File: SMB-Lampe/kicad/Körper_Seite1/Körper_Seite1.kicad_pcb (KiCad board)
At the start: 2 copper layers, 123 x 95.7 mm, 24 parts, among them J1 Conn_01x01_Pin, J2 Conn_01x01_Pin, J3 Conn_01x01_Pin, J4 Conn_01x01_Pin, J5 Conn_01x01_Pin, J6 Conn_01x01_Pin

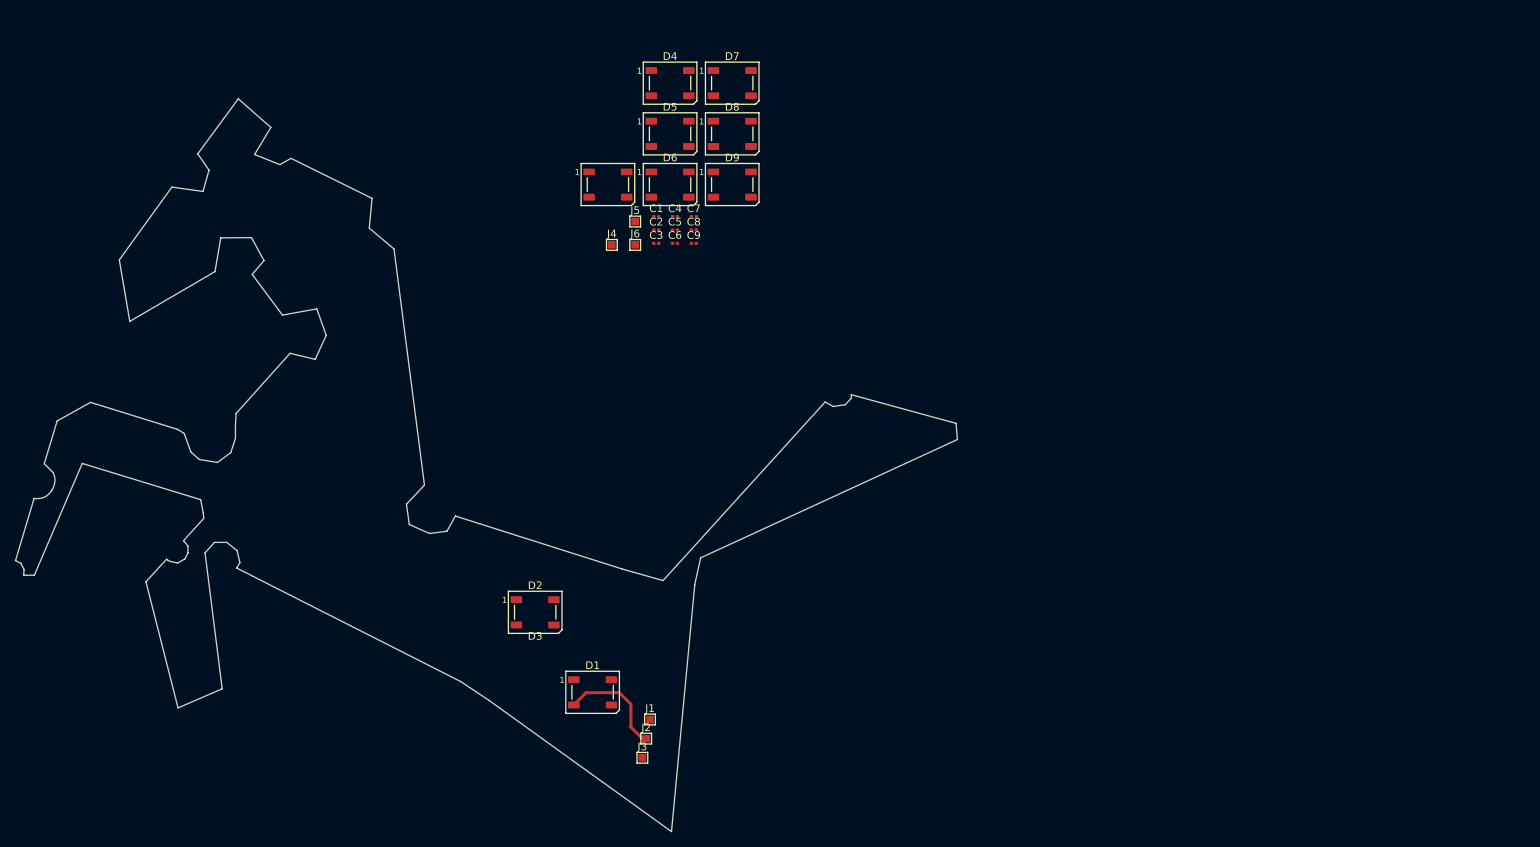
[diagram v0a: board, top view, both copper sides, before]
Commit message: Platine für Körper Seite 1 erfolgreich erstellt
Die Platine wurde mit der alten Außenkontur erstellt und fast komplett erfolgreich die Leiterbahnen erstellt.
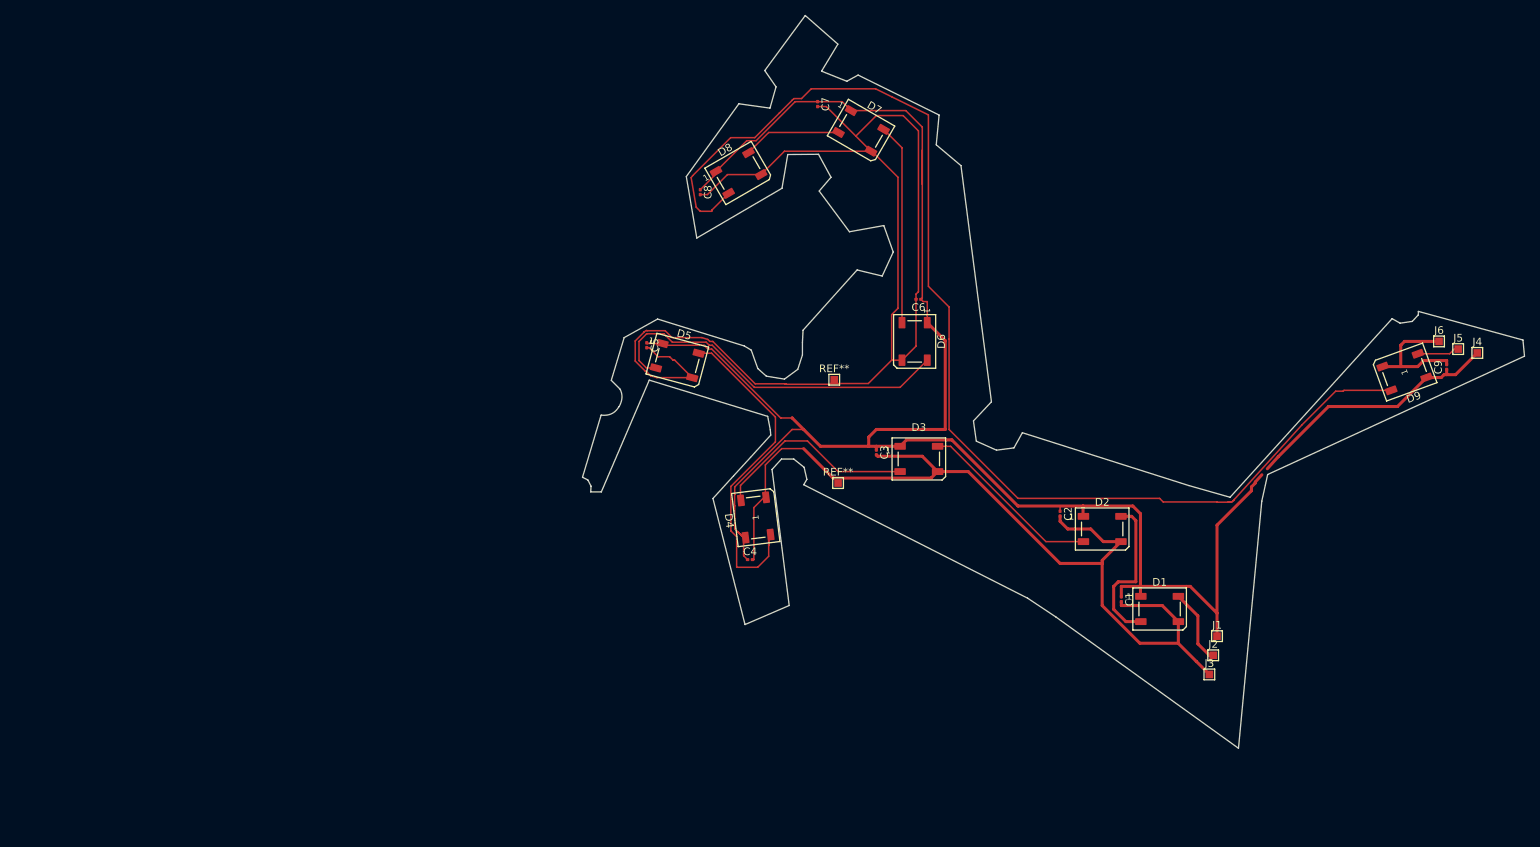
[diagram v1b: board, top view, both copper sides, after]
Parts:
- added REF**: TestPoint_Pad_1.0x1.0mm, TestPoint:TestPoint_Pad_1.0x1.0mm, F.Cu at (188.1, 95.1)
- added REF**: TestPoint_Pad_1.0x1.0mm, TestPoint:TestPoint_Pad_1.0x1.0mm, F.Cu at (187.6, 81.6)
- moved J4 113.9 mm to (271.6, 78.1)
- moved J5 108.8 mm to (269.1, 77.6)
- moved J6 105.8 mm to (266.6, 76.6)
- moved C9 99.7 mm to (267.6, 80.0), turned to 90 degrees
- moved D9 91.2 mm to (262.1, 80.6), turned to -160 degrees
- moved C1 78.7 mm to (225.1, 110.3), turned to -90 degrees
- moved D1 74.9 mm to (230.1, 111.6)
- moved D2 74.9 mm to (222.6, 101.1)
- moved J1 74.9 mm to (237.6, 115.1)
- moved J2 74.9 mm to (237.1, 117.6)
- moved J3 74.9 mm to (236.6, 120.1)
- moved C2 64.5 mm to (217.1, 99.1), turned to -90 degrees
- moved D4 57.8 mm to (177.3, 99.6), turned to 97 degrees
- moved D3 54.2 mm to (198.6, 92.0)
- moved C4 45.9 mm to (176.6, 105.1)
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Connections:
- D1 pad 2: /Data_In -> Net-(D1-DOUT)
- D1 pad 4: Net-(D1-DIN) -> /Data_In
- D2 pad 2: Net-(D1-DIN) -> Net-(D2-DOUT)
- D2 pad 4: Net-(D2-DIN) -> Net-(D1-DOUT)
- D3 pad 2: Net-(D2-DIN) -> Net-(D3-DOUT)
- D3 pad 4: Net-(D3-DIN) -> Net-(D2-DOUT)
- D4 pad 2: Net-(D3-DIN) -> Net-(D4-DOUT)
- D4 pad 4: Net-(D4-DIN) -> Net-(D3-DOUT)
- D5 pad 2: Net-(D4-DIN) -> Data
- D5 pad 4: Data -> Net-(D4-DOUT)
- D6 pad 2: Data -> Net-(D6-DOUT)
- D6 pad 4: Net-(D6-DIN) -> Data
- D7 pad 2: Net-(D6-DIN) -> Net-(D7-DOUT)
- D7 pad 4: Net-(D7-DIN) -> Net-(D6-DOUT)
- D8 pad 2: Net-(D7-DIN) -> Net-(D8-DOUT)
- D8 pad 4: Net-(D8-DIN) -> Net-(D7-DOUT)
- D9 pad 2: Net-(D8-DIN) -> /Data_OUT
- D9 pad 4: /Data_OUT -> Net-(D8-DOUT)
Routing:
- net GND: track 0.00 -> 301.9 mm
- net +5V: track 0.00 -> 283.3 mm
- net Net-(D8-DOUT): track 0.00 -> 156.3 mm
- net Data: track 0.00 -> 47.5 mm
- net Net-(D4-DOUT): track 0.00 -> 44.8 mm
- net Net-(D3-DOUT): track 0.00 -> 26.7 mm
- net Net-(D6-DOUT): track 0.00 -> 26.2 mm
- net Net-(D2-DOUT): track 0.00 -> 24.2 mm
- net Net-(D1-DOUT): track 0.00 -> 20.5 mm
- net Net-(D7-DOUT): track 0.00 -> 12.9 mm
- net /Data_OUT: track 0.00 -> 5.52 mm
- net /Data_In: track 14.4 -> 9.88 mm
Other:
- board size 123 x 95.7 mm -> 123.1 x 95.7 mm

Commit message: Hinterbein Seite 1/2 erstellt
Anschlüsse zwischen den Platinen mit MountingHoles. Eigenes MountingHole Erstellt
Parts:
- moved J4 128.4 mm to (143.3, 83.4)
- moved J5 128.4 mm to (140.8, 82.9)
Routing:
- net /Data_OUT: track 5.52 -> 54.0 mm
- net +5V: track 283.3 -> 325.1 mm
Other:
- board size 123.1 x 95.7 mm -> 252 x 99.5 mm

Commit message: Vorderseite Platine Körper Seite 1 fertig
zwei GND Verbindungen fehlen noch
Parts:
- removed J4, J5, J6: Conn_01x01_Pin, TestPoint:TestPoint_Pad_1.0x1.0mm
- removed REF** (x2): TestPoint_Pad_1.0x1.0mm, TestPoint:TestPoint_Pad_1.0x1.0mm
- added H1: MountingHole_Pad, Eigenen_Library:MountingHole D2 x d1 test, F.Cu at (189.0, 101.0)
- added H2: MountingHole_Pad, Eigenen_Library:MountingHole D2 x d1 test, F.Cu at (186.0, 100.0)
- added H3: MountingHole_Pad, Eigenen_Library:MountingHole D2 x d1 test, F.Cu at (183.0, 99.0)
- J1, J2, J3: footprint TestPoint:TestPoint_Pad_1.0x1.0mm -> TestPoint:TestPoint_Pad_2.0x2.0mm
- moved C3 89.5 mm to (106.0, 112.0)
- moved D3 89.5 mm to (111.5, 112.5)
- moved J3 88.7 mm to (151.0, 143.5)
- moved C5 88.4 mm to (77.8, 100.4), turned to -109 degrees
- moved D6 88.1 mm to (112.5, 97.5)
- moved J2 88.0 mm to (152.0, 140.0)
- moved C6 87.9 mm to (113.2, 92.0)
- moved D9 87.9 mm to (177.5, 104.5), turned to -154 degrees
- moved D5 87.8 mm to (82.2, 102.0), turned to -18 degrees
- moved C2 87.7 mm to (132.5, 122.5)
- moved D4 87.7 mm to (92.7, 122.8)
- moved D7 87.6 mm to (106.5, 72.0), turned to -45 degrees
- moved C9 87.5 mm to (183.0, 102.5), turned to 115 degrees
- moved D8 87.5 mm to (90.8, 78.4), turned to 29 degrees
- moved D2 87.4 mm to (138.0, 123.0)
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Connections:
- net /Data_In renamed /Data_In__Hinterbein_hinten_Seite2
- D9 pad 2: /Data_OUT -> /Data_OUT_Körper_Seite2
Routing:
- net /Data_OUT: track 54.0 -> 0.00 mm
- net +5V: track 325.1 -> 285.8 mm
- net /Data_OUT_Körper_Seite2: track 0.00 -> 7.83 mm
- net Net-(D4-DOUT): track 44.8 -> 51.3 mm
- net GND: track 301.9 -> 295.6 mm
- net Net-(D2-DOUT): track 24.2 -> 29.5 mm
- net Net-(D3-DOUT): track 26.7 -> 21.8 mm
- net Net-(D6-DOUT): track 26.2 -> 23.1 mm
- net Data: track 47.5 -> 49.9 mm
- net Net-(D1-DOUT): track 20.5 -> 22.8 mm
- net Net-(D8-DOUT): track 156.3 -> 157.8 mm
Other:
- board size 252 x 99.5 mm -> 121.9 x 96.3 mm
- board text added: "-155°"
- board text added: "-18°"
- board text added: "29°"
- board text added: "97°"

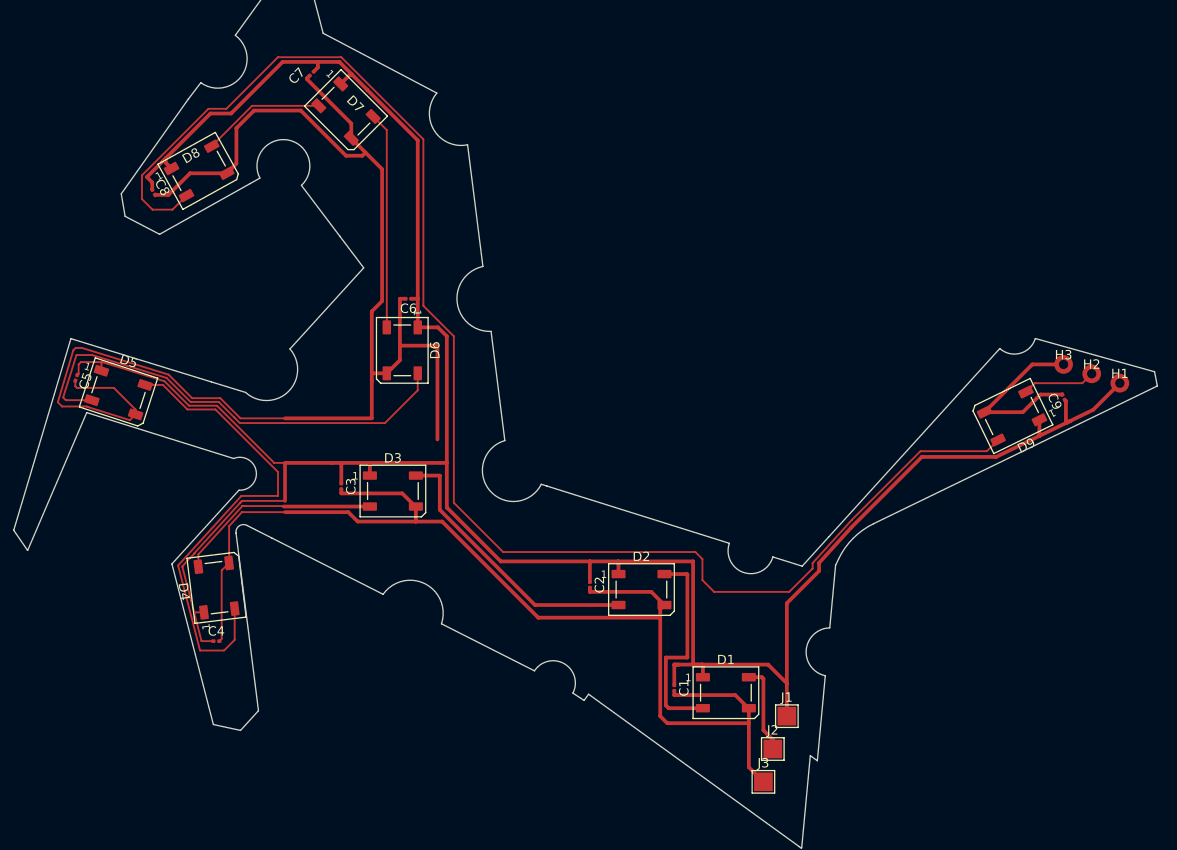
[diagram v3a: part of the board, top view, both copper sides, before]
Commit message: Körper mit Vorder und Rückseite fertig
Alle Leiterbahnen sind gelegt und Verbindungen zu den anderen Platinen platziert
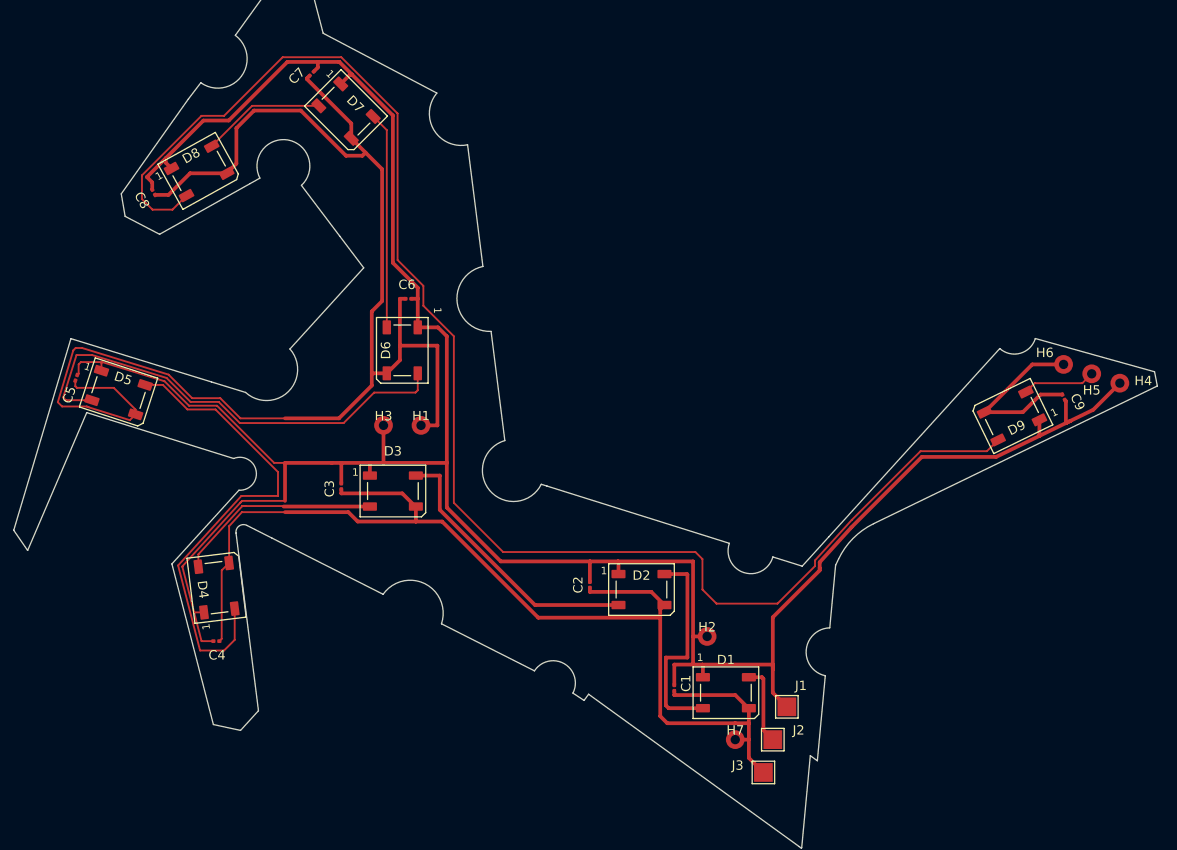
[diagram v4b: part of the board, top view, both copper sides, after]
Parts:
- added H1: MountingHole_Pad, Eigenen_Library:MountingHole D2 x d1 test, F.Cu at (114.5, 105.5)
- added H2: MountingHole_Pad, Eigenen_Library:MountingHole D2 x d1 test, F.Cu at (145.0, 128.0)
- added H3: MountingHole_Pad, Eigenen_Library:MountingHole D2 x d1 test, F.Cu at (110.5, 105.5)
- added H7: MountingHole_Pad, Eigenen_Library:MountingHole D2 x d1 test, F.Cu at (148.0, 139.0)
- moved J1 1.00 mm to (153.5, 135.5)
- moved J2 1.00 mm to (152.0, 139.0)
- moved J3 1.00 mm to (151.0, 142.5)
- renumbered H1 to H4, H2 to H5, H3 to H6
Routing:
- net +5V: track 285.8 -> 288.2 mm
- net Net-(D8-DOUT): track 157.8 -> 159.4 mm
- net GND: track 295.6 -> 294.2 mm
- net /Data_In__Hinterbein_hinten_Seite2: track 9.53 -> 8.53 mm

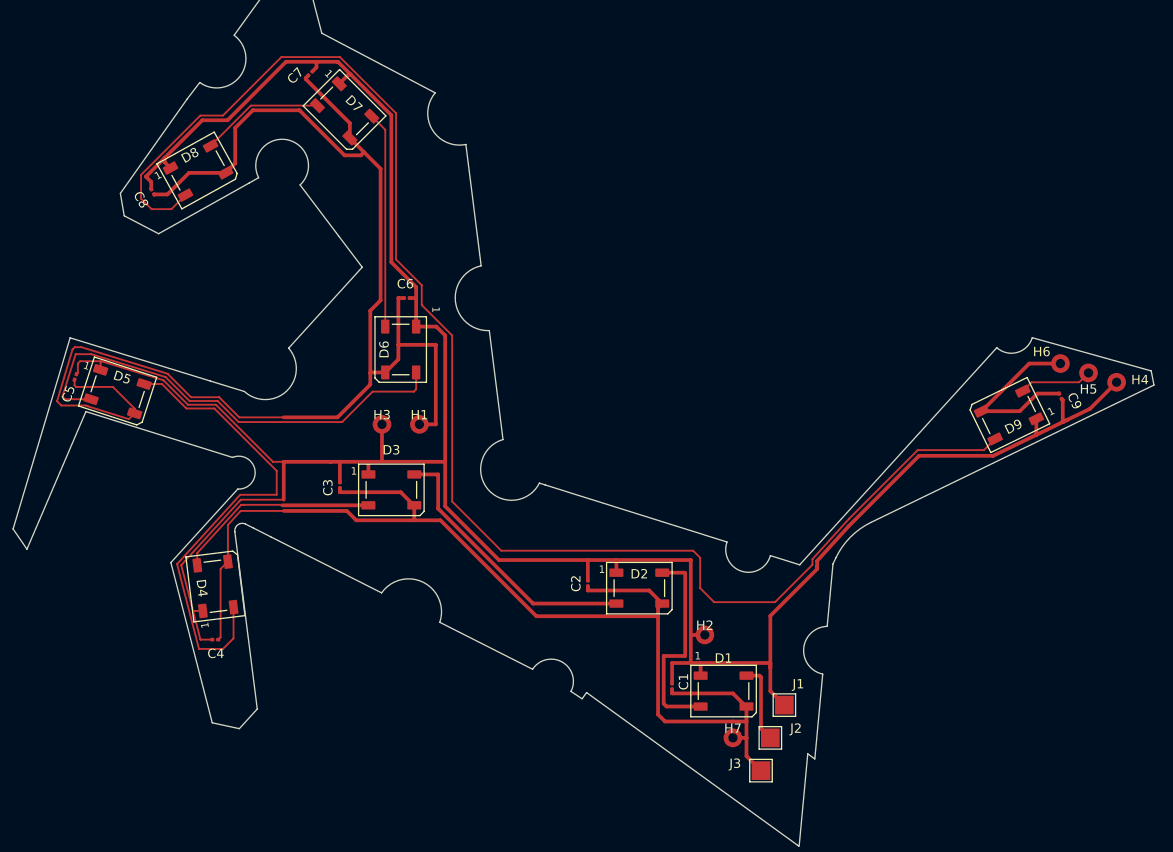
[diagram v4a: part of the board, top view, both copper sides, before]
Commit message: Vorderes Hinterbein fertig
Alle Platinen sind fertig beschaltet
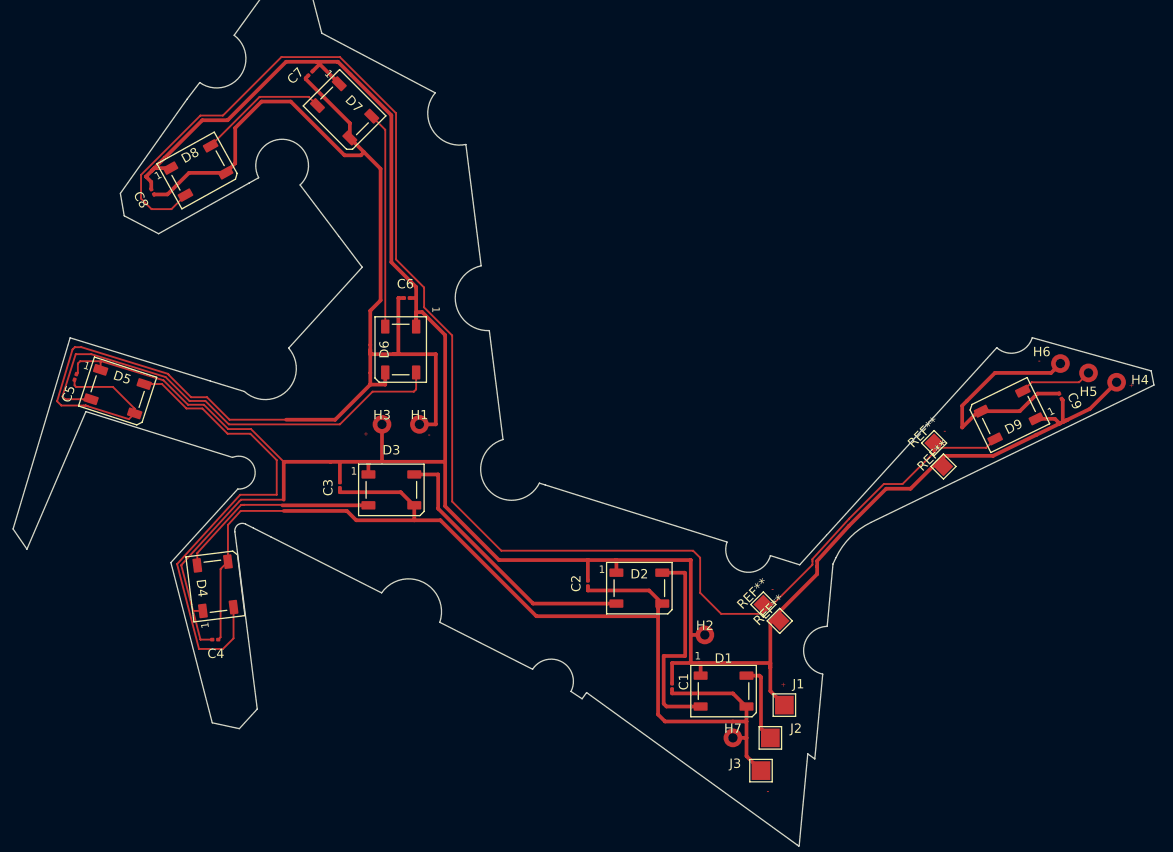
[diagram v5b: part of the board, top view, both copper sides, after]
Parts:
- added REF**: TestPoint_Pad_1.5x1.5mm, TestPoint:TestPoint_Pad_1.5x1.5mm, F.Cu at (153.0, 126.5)
- added REF**: TestPoint_Pad_1.5x1.5mm, TestPoint:TestPoint_Pad_1.5x1.5mm, F.Cu at (170.5, 110.0)
- added REF**: TestPoint_Pad_1.5x1.5mm, TestPoint:TestPoint_Pad_1.5x1.5mm, F.Cu at (169.5, 107.5)
- added REF**: TestPoint_Pad_1.5x1.5mm, TestPoint:TestPoint_Pad_1.5x1.5mm, F.Cu at (151.2, 124.8)
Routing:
- net GND: track 294.2 -> 303.9 mm
- net +5V: track 288.2 -> 293.8 mm
- net Net-(D8-DOUT): track 159.4 -> 160.7 mm
- net Net-(D7-DOUT): track 13.2 -> 14.0 mm
- net Net-(D4-DOUT): track 51.3 -> 52.0 mm
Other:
- board text added: "+"
- board text added: "-"
